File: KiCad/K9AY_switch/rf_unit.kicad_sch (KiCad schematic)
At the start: 31 parts, among them J3 LOOPS, J7 MANUAL_SWITCH, K1 G5V-2, K10 TIANBO-HJR-4102-L, K2 G5V-2, K3 Tianbo HJR 1-2C-12V, K4 G5V-2, K5 TIANBO-HJR-4102-L, K6 TIANBO-HJR-4102-L, K7 TIANBO-HJR-4102-L, K8 TIANBO-HJR-4102-L, K9 TIANBO-HJR-4102-L

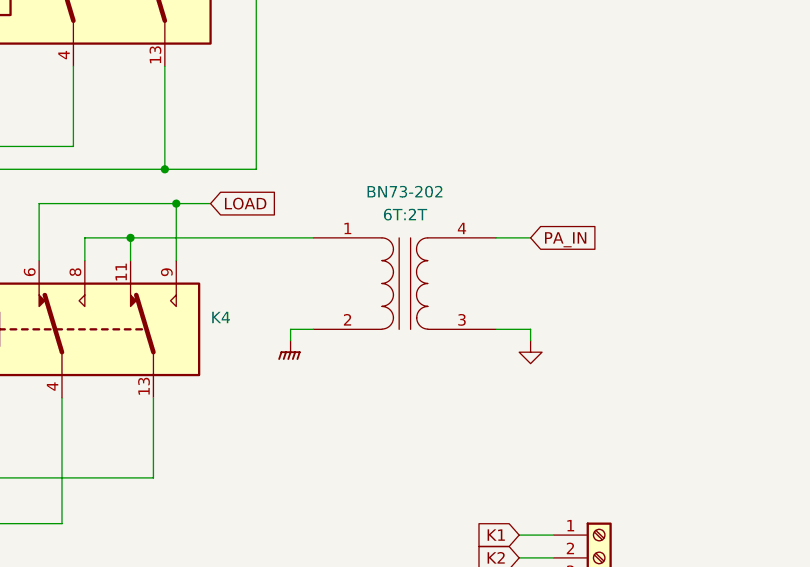
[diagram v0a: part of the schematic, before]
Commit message: Update KiCad project, gerbers and pictures
- updated schematic, PCB, BOM, gerbers and plots
- new photos: k1, mosfet, pwr; updated direction diagram
- ignore KiCad backups, *.tar.gz and k9ay_v5.zip

Co-Authored-By: Claude Opus 5.5 <noreply@anthropic.com>
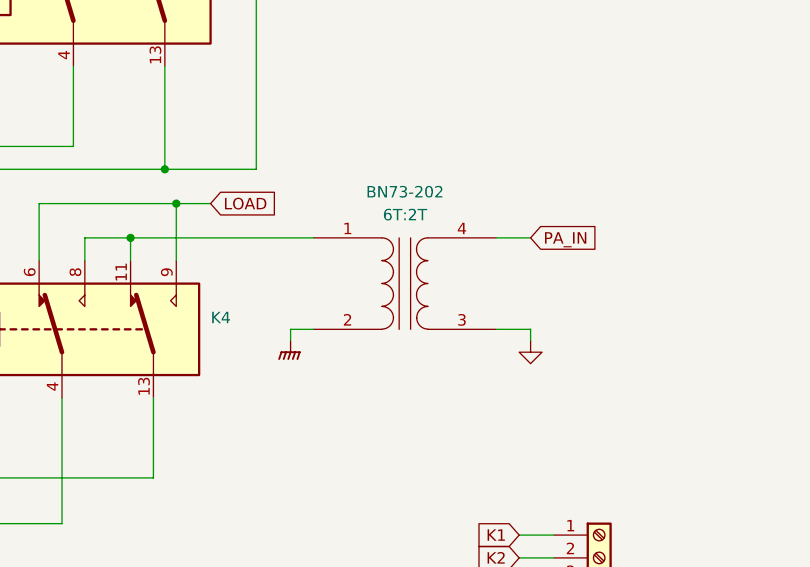
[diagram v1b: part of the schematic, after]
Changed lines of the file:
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@@
 (kicad_sch
-	(version 20231120)
+	(version 20250114)
 	(generator "eeschema")
-	(generator_version "8.0")
+	(generator_version "9.0")
 	(paper "A4")
 	(title_block
 		(title "RF unit")
 		(date "2025-02-05")
+	)
+	(text "Active level - GND"
+		(exclude_from_sim no)
+		(at 229.87 161.29 0)
+		(effects
+			(font
+				(size 1.27 1.27)
+			)
+		)
 	)
 	(junction
@@
 		)
 	)
-	(text "Active level - GND"
-		(exclude_from_sim no)
-		(at 229.87 161.29 0)
-		(effects
-			(font
-				(size 1.27 1.27)
-			)
-		)
-	)
